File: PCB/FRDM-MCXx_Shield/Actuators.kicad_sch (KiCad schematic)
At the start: 22 parts, among them M1 Motor_Servo, U3 STPIC6C595MTR, U4 SN74LV164ADR

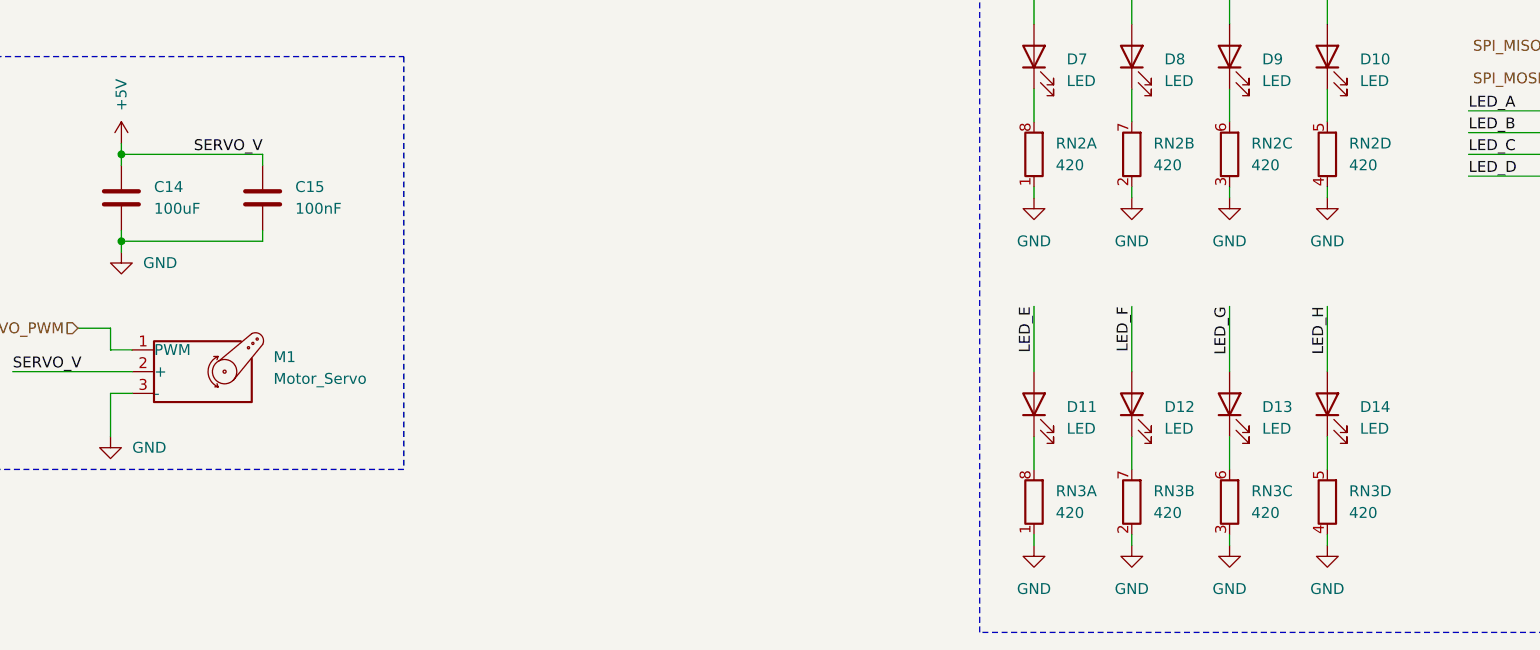
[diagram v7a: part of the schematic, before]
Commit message: Updated PCB and added bill of materials
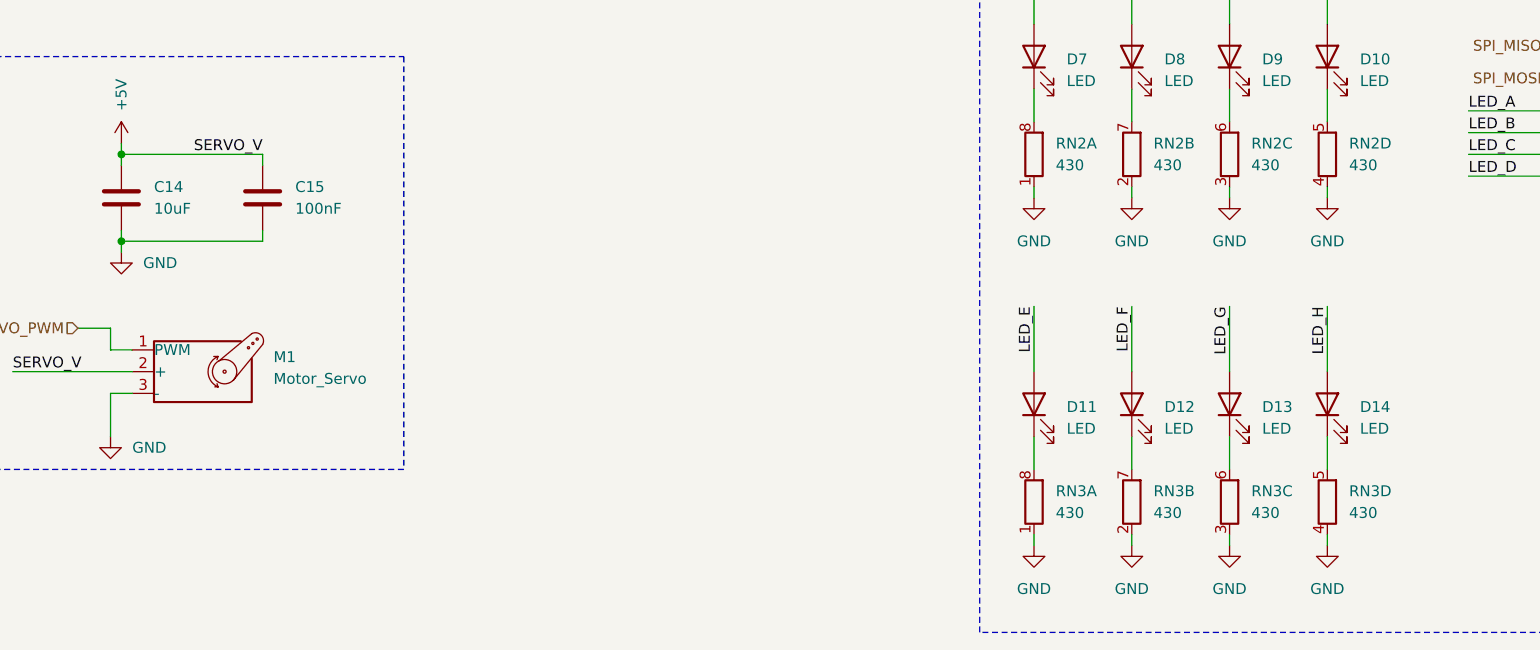
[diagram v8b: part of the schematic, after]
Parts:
- C10, C11, C12, C13, C15: GPN (none) -> GPC0603104
- C14: value 100uF -> 10uF; GPN (none) -> GPC0603106
- M1: GPN (none) -> GPHA-1X03
- RN2, RN3: value 420 -> 430
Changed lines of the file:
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@@
       (effects (font (size 1.27 1.27)) (justify left))
     )
-    (property "Value" "420" (at 161.29 106.68 0)
+    (property "Value" "430" (at 161.29 106.68 0)
       (effects (font (size 1.27 1.27)) (justify left))
     )
@@
       (effects (font (size 1.27 1.27)) (justify left))
     )
-    (property "Value" "420" (at 184.15 106.68 0)
+    (property "Value" "430" (at 184.15 106.68 0)
       (effects (font (size 1.27 1.27)) (justify left))
     )
@@
       (effects (font (size 1.27 1.27)) hide)
     )
+    (property "GPN" "GPC0603104" (at 251.46 87.63 90)
+      (effects (font (size 1.27 1.27)) hide)
+    )
     (pin "2")
     (pin "1")
@@
       (effects (font (size 1.27 1.27)) (justify left))
     )
-    (property "Value" "420" (at 149.86 147.32 0)
+    (property "Value" "430" (at 149.86 147.32 0)
       (effects (font (size 1.27 1.27)) (justify left))
     )
@@
       (effects (font (size 1.27 1.27)) (justify right))
     )
-    (property "Value" "100uF" (at 44.45 111.76 0)
+    (property "Value" "10uF" (at 44.45 111.76 0)
       (effects (font (size 1.27 1.27)) (justify right))
     )
@@
       (effects (font (size 1.27 1.27)) hide)
     )
+    (property "GPN" "GPC0603106" (at 40.64 110.49 0)
+      (effects (font (size 1.27 1.27)) hide)
+    )
     (pin "2")
     (pin "1")
@@
       (effects (font (size 1.27 1.27)) (justify left))
     )
-    (property "Value" "420" (at 149.86 106.68 0)
+    (property "Value" "430" (at 149.86 106.68 0)
       (effects (font (size 1.27 1.27)) (justify left))
     )
@@
       (effects (font (size 1.27 1.27)) (justify left))
     )
-    (property "Value" "420" (at 161.29 147.32 0)
+    (property "Value" "430" (at 161.29 147.32 0)
       (effects (font (size 1.27 1.27)) (justify left))
     )
@@
       (effects (font (size 1.27 1.27)) hide)
     )
+    (property "GPN" "GPC0603104" (at 111.76 54.61 90)
+      (effects (font (size 1.27 1.27)) hide)
+    )
     (pin "2")
     (pin "1")
@@
       (effects (font (size 1.27 1.27)) (justify left))
     )
-    (property "Value" "420" (at 172.72 106.68 0)
+    (property "Value" "430" (at 172.72 106.68 0)
       (effects (font (size 1.27 1.27)) (justify left))
     )
@@
       (effects (font (size 1.27 1.27)) hide)
     )
+    (property "GPN" "GPC0603104" (at 83.82 54.61 90)
+      (effects (font (size 1.27 1.27)) hide)
+    )
     (pin "2")
     (pin "1")
@@
       (effects (font (size 1.27 1.27)) hide)
     )
+    (property "GPN" "GPC0603104" (at 57.15 110.49 0)
+      (effects (font (size 1.27 1.27)) hide)
+    )
     (pin "2")
     (pin "1")
@@
       (effects (font (size 1.27 1.27)) (justify left))
     )
-    (property "Value" "420" (at 172.72 147.32 0)
+    (property "Value" "430" (at 172.72 147.32 0)
       (effects (font (size 1.27 1.27)) (justify left))
     )
@@
       (effects (font (size 1.27 1.27)) (justify left))
     )
-    (property "Value" "420" (at 184.15 147.32 0)
+    (property "Value" "430" (at 184.15 147.32 0)
       (effects (font (size 1.27 1.27)) (justify left))
     )
@@
       (effects (font (size 1.27 1.27)) hide)
     )
+    (property "GPN" "GPHA-1X03" (at 49.53 130.81 0)
+      (effects (font (size 1.27 1.27)) hide)
+    )
     (pin "2")
     (pin "3")
@@
       (effects (font (size 1.27 1.27)) hide)
     )
+    (property "GPN" "GPC0603104" (at 55.88 54.61 90)
+      (effects (font (size 1.27 1.27)) hide)
+    )
